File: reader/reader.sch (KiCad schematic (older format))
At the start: 63 parts, among them J1 USB_B_Mini, J2 swd, J3 Conn_01x06, J4 v_sup, Q1 CPH3350-TL-W, SW1 SW_Push, U1 BA33BC0FP-E2, U2 ST25R95, U3 STM32G051GxU, U4 FC2004C03-NSWBBW-91*E, Y1 27.12MHz

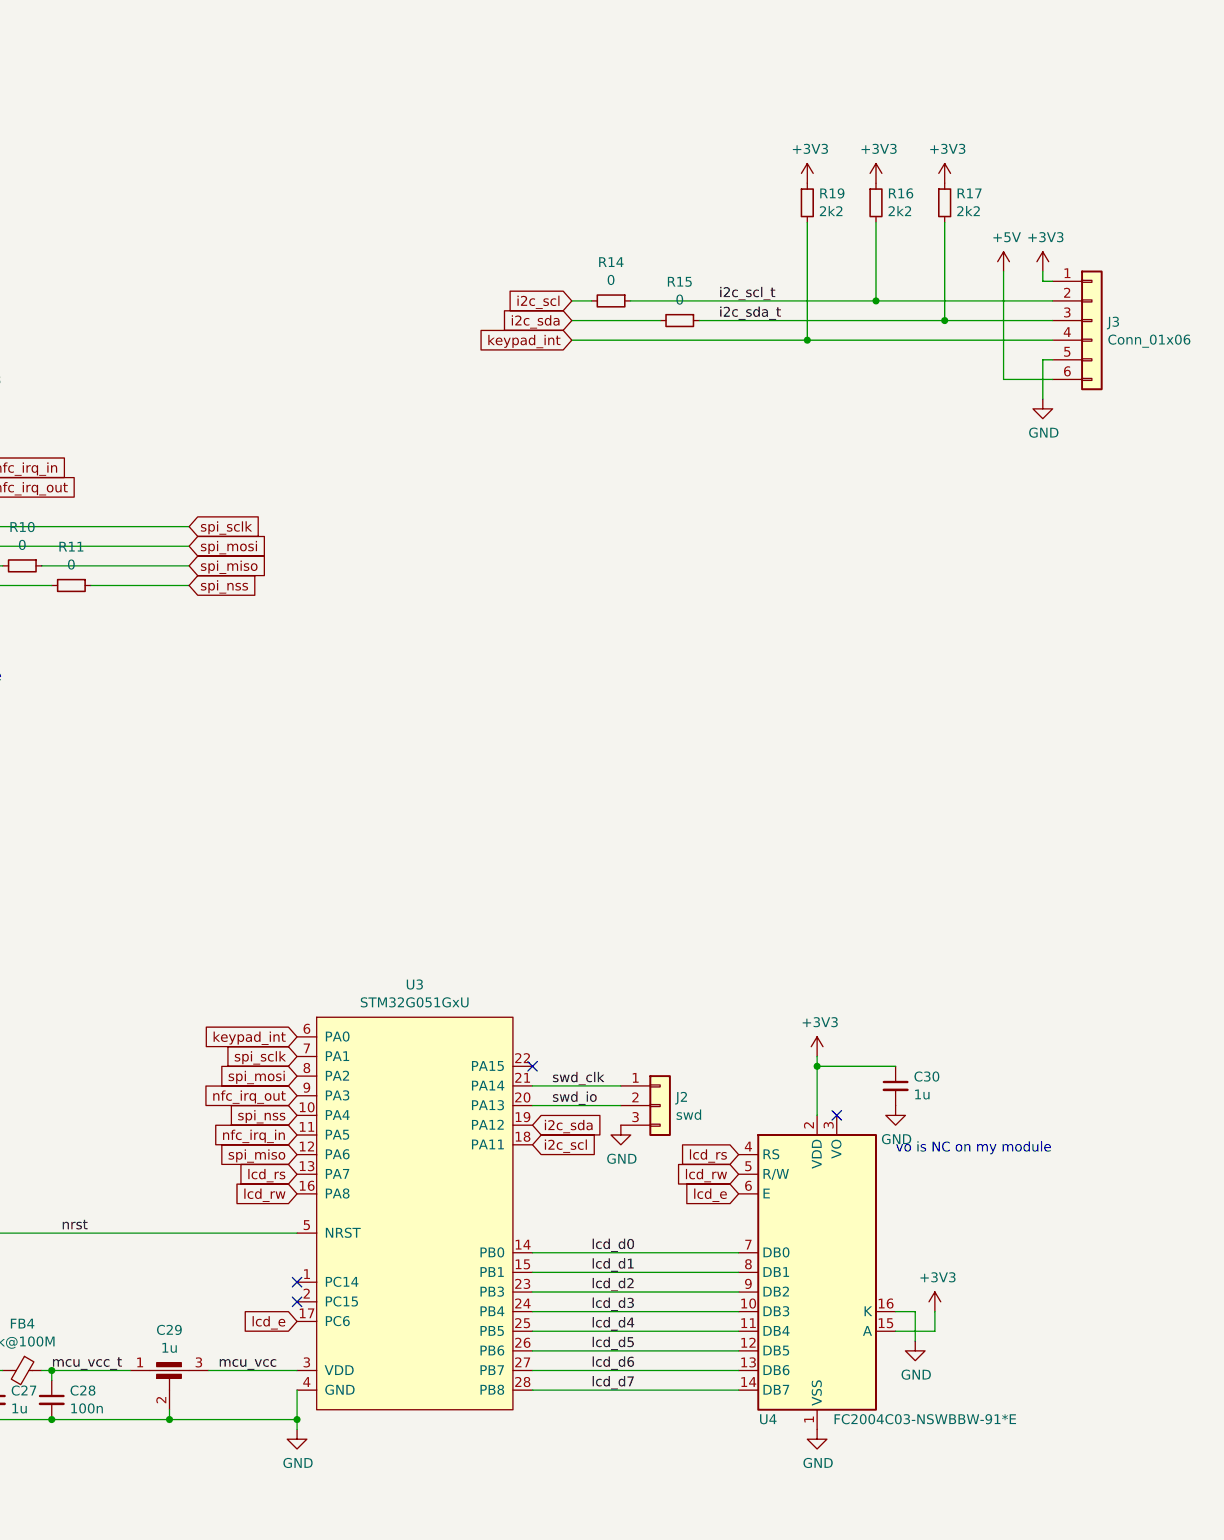
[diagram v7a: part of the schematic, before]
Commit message: Add proper mcu pinout and uart as output
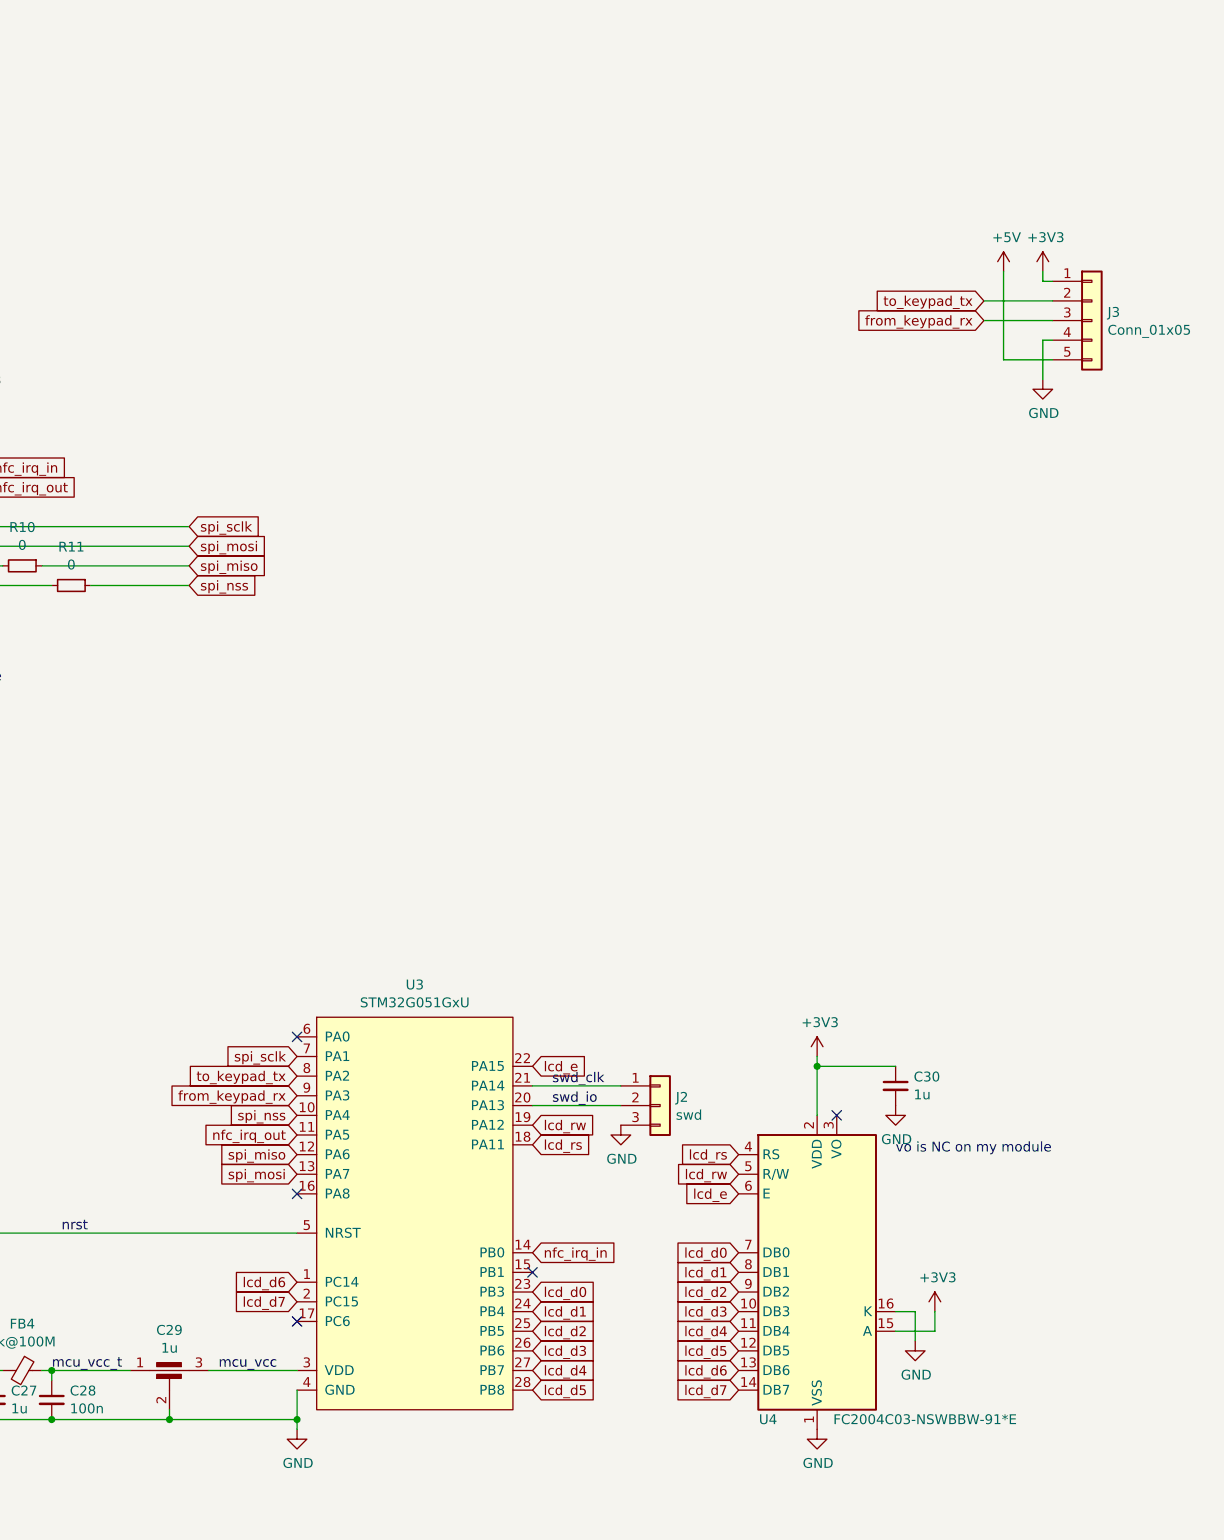
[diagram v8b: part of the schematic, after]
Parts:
- removed J3: Conn_01x06, Connector_PinHeader_2.54mm:PinHeader_1x06_P2.54mm_Vertical, symbol Connector_Generic:Conn_01x06
- removed R14, R15: 0, Resistor_SMD:R_0603_1608Metric_Pad1.05x0.95mm_HandSolder, symbol Device:R_Small
- removed R16, R17, R19: 2k2, Resistor_SMD:R_0603_1608Metric_Pad1.05x0.95mm_HandSolder, symbol Device:R_Small
- added J3: Conn_01x05, Connector_PinHeader_2.54mm:PinHeader_1x05_P2.54mm_Vertical, symbol Connector_Generic:Conn_01x05
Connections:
- net i2c_scl is gone; now on net lcd_rs: U3.18 (PA11)
- net i2c_sda is gone; now on net lcd_rw: U3.19 (PA12)
- net +3V3: now also J3.1 (Pin_1)
- net +5V: now also J3.5 (Pin_5)
- net GND: now also J3.4 (Pin_4)
- net lcd_d0: now also U3.23 (PB3); no longer U3.14 (PB0)
- net lcd_d1: now also U3.24 (PB4); no longer U3.15 (PB1)
- net lcd_d2: now also U3.25 (PB5); no longer U3.23 (PB3)
- net lcd_d3: now also U3.26 (PB6); no longer U3.24 (PB4)
- net lcd_d4: now also U3.27 (PB7); no longer U3.25 (PB5)
- net lcd_d5: now also U3.28 (PB8); no longer U3.26 (PB6)
- net lcd_d6: now also U3.1 (PC14); no longer U3.27 (PB7)
- net lcd_d7: now also U3.2 (PC15); no longer U3.28 (PB8)
- net lcd_e: now also U3.22 (PA15); no longer U3.17 (PC6)
- net lcd_rs: no longer U3.13 (PA7)
- net lcd_rw: no longer U3.16 (PA8)
- net nfc_irq_in: now also U3.14 (PB0); no longer U3.11 (PA5)
- net nfc_irq_out: now also U3.11 (PA5); no longer U3.9 (PA3)
- net spi_mosi: now also U3.13 (PA7); no longer U3.8 (PA2)
- net keypad_int: no longer names the net of U3.6 (PA0)
- new net from_keypad_rx: J3.3 (Pin_3), U3.9 (PA3)
- new net to_keypad_tx: J3.2 (Pin_2), U3.8 (PA2)
- no-connect marks 5 -> 6
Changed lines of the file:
@@
 	1    0    0    -1
 $EndComp
-Text GLabel 12050 2650 0    50   Input ~ 0
-i2c_sda
-Text GLabel 12050 2550 0    50   Input ~ 0
-i2c_scl
-$Comp
-L power:+3V3 #PWR031
-U 1 1 617ACEE2
-P 13600 1950
-F 0 "#PWR031" H 13600 1800 50  0001 C CNN
-F 1 "+3V3" H 13615 2123 50  0000 C CNN
-F 2 "" H 13600 1950 50  0001 C CNN
-F 3 "" H 13600 1950 50  0001 C CNN
-	1    13600 1950
-	1    0    0    -1
-$EndComp
-$Comp
-L Device:R_Small R16
-U 1 1 617AD187
-P 13600 2050
-F 0 "R16" H 13659 2096 50  0000 L CNN
-F 1 "2k2" H 13659 2005 50  0000 L CNN
-F 2 "Resistor_SMD:R_0603_1608Metric_Pad1.05x0.95mm_HandSolder" H 13600 2050 50  0001 C CNN
-F 3 "~" H 13600 2050 50  0001 C CNN
-	1    13600 2050
-	1    0    0    -1
-$EndComp
-$Comp
-L power:+3V3 #PWR032
-U 1 1 617B431C
-P 13950 1950
-F 0 "#PWR032" H 13950 1800 50  0001 C CNN
-F 1 "+3V3" H 13965 2123 50  0000 C CNN
-F 2 "" H 13950 1950 50  0001 C CNN
-F 3 "" H 13950 1950 50  0001 C CNN
-	1    13950 1950
-	1    0    0    -1
-$EndComp
-$Comp
-L Device:R_Small R17
-U 1 1 617B4322
-P 13950 2050
-F 0 "R17" H 14009 2096 50  0000 L CNN
-F 1 "2k2" H 14009 2005 50  0000 L CNN
-F 2 "Resistor_SMD:R_0603_1608Metric_Pad1.05x0.95mm_HandSolder" H 13950 2050 50  0001 C CNN
-F 3 "~" H 13950 2050 50  0001 C CNN
-	1    13950 2050
-	1    0    0    -1
-$EndComp
-Wire Wire Line
-	13600 2150 13600 2550
 $Comp
 L power:GND #PWR034
 U 1 1 617F51EA
-P 14450 3050
-F 0 "#PWR034" H 14450 2800 50  0001 C CNN
-F 1 "GND" H 14455 2877 50  0000 C CNN
-F 2 "" H 14450 3050 50  0001 C CNN
-F 3 "" H 14450 3050 50  0001 C CNN
-	1    14450 3050
-	1    0    0    -1
-$EndComp
-Text GLabel 12050 2750 0    50   Input ~ 0
-keypad_int
-Wire Wire Line
-	13950 2150 13950 2650
+P 14450 2950
+F 0 "#PWR034" H 14450 2700 50  0001 C CNN
+F 1 "GND" H 14455 2777 50  0000 C CNN
+F 2 "" H 14450 2950 50  0001 C CNN
+F 3 "" H 14450 2950 50  0001 C CNN
+	1    14450 2950
+	1    0    0    -1
+$EndComp
 $Comp
 L Connector_Generic:Conn_01x02 J4
@@
 Wire Wire Line
 	7300 4900 7400 4900
-Text GLabel 10650 6300 0    50   Input ~ 0
-keypad_int
-NoConn ~ 11850 6450
 Wire Wire Line
 	10200 8000 10650 8000
@@
 Text Label 10250 8000 0    50   ~ 0
 mcu_vcc
-Text GLabel 11850 6850 2    50   Input ~ 0
-i2c_scl
-Text GLabel 11850 6750 2    50   Input ~ 0
-i2c_sda
 Text Label 11950 6650 0    50   ~ 0
 swd_io
@@
 Wire Wire Line
 	10650 8100 10650 8250
-Text GLabel 10650 7750 0    50   Input ~ 0
-lcd_e
-Text GLabel 10650 7100 0    50   Input ~ 0
+Text GLabel 11850 6750 2    50   Input ~ 0
 lcd_rw
-Text GLabel 10650 7000 0    50   Input ~ 0
+Text GLabel 11850 6850 2    50   Input ~ 0
 lcd_rs
-Text Label 12150 8100 0    50   ~ 0
-lcd_d7
-Text Label 12150 8000 0    50   ~ 0
-lcd_d6
-Text Label 12150 7900 0    50   ~ 0
-lcd_d5
-Text Label 12150 7800 0    50   ~ 0
-lcd_d4
-Text Label 12150 7700 0    50   ~ 0
-lcd_d3
-Text Label 12150 7600 0    50   ~ 0
-lcd_d2
-Text Label 12150 7500 0    50   ~ 0
-lcd_d1
-Text Label 12150 7400 0    50   ~ 0
-lcd_d0
+Text GLabel 11850 7400 2    50   Input ~ 0
+nfc_irq_in
 Text GLabel 10650 6800 0    50   Input ~ 0
-nfc_irq_in
-Text GLabel 10650 6600 0    50   Input ~ 0
 nfc_irq_out
 Text GLabel 10650 6900 0    50   Input ~ 0
@@
 Text GLabel 10650 6700 0    50   Input ~ 0
 spi_nss
-Text GLabel 10650 6500 0    50   Input ~ 0
+Text GLabel 10650 7000 0    50   Input ~ 0
 spi_mosi
 Text GLabel 10650 6400 0    50   Input ~ 0
 spi_sclk
-Wire Wire Line
-	11850 8100 12900 8100
-Wire Wire Line
-	12900 8000 11850 8000
-Wire Wire Line
-	11850 7900 12900 7900
-Wire Wire Line
-	11850 7800 12900 7800
-Wire Wire Line
-	12900 7700 11850 7700
-Wire Wire Line
-	11850 7600 12900 7600
-Wire Wire Line
-	12900 7500 11850 7500
-Wire Wire Line
-	11850 7400 12900 7400
 Wire Wire Line
 	8100 7300 8100 7350
@@
 	1    0    0    -1
 $EndComp
-$Comp
-L Connector_Generic:Conn_01x06 J3
-U 1 1 61680C40
-P 14700 2650
-F 0 "J3" H 14780 2642 50  0000 L CNN
-F 1 "Conn_01x06" H 14780 2551 50  0000 L CNN
-F 2 "Connector_PinHeader_2.54mm:PinHeader_1x06_P2.54mm_Vertical" H 14700 2650 50  0001 C CNN
-F 3 "~" H 14700 2650 50  0001 C CNN
-	1    14700 2650
-	1    0    0    -1
-$EndComp
 Wire Wire Line
 	14450 2450 14450 2400
@@
 	14450 2450 14500 2450
 Wire Wire Line
-	13600 2550 14500 2550
-Wire Wire Line
-	13950 2650 14500 2650
-Wire Wire Line
 	7650 2900 8100 2900
 Wire Wire Line
@@
 Wire Wire Line
 	4200 1350 4600 1350
-Wire Wire Line
-	14450 3050 14450 2850
-Wire Wire Line
-	14450 2850 14500 2850
-Wire Wire Line
-	14500 2950 14250 2950
-Wire Wire Line
-	14250 2400 14250 2950
-NoConn ~ 10650 7550
-NoConn ~ 10650 7650
 Wire Wire Line
 	8600 7300 10650 7300
@@
 Wire Wire Line
 	10000 8250 10650 8250
-Text Label 12800 2650 0    50   ~ 0
-i2c_sda_t
-Text Label 12800 2550 0    50   ~ 0
-i2c_scl_t
-Wire Wire Line
-	12500 2650 12050 2650
-Wire Wire Line
-	12150 2550 12050 2550
-$Comp
-L Device:R_Small R15
-U 1 1 617FEC6C
-P 12600 2650
-F 0 "R15" V 12404 2650 50  0000 C CNN
-F 1 "0" V 12495 2650 50  0000 C CNN
-F 2 "Resistor_SMD:R_0603_1608Metric_Pad1.05x0.95mm_HandSolder" H 12600 2650 50  0001 C CNN
-F 3 "~" H 12600 2650 50  0001 C CNN
-	1    12600 2650
-	0    1    1    0
-$EndComp
-$Comp
-L Device:R_Small R14
-U 1 1 617FEA2B
-P 12250 2550
-F 0 "R14" V 12054 2550 50  0000 C CNN
-F 1 "0" V 12145 2550 50  0000 C CNN
-F 2 "Resistor_SMD:R_0603_1608Metric_Pad1.05x0.95mm_HandSolder" H 12250 2550 50  0001 C CNN
-F 3 "~" H 12250 2550 50  0001 C CNN
-	1    12250 2550
-	0    1    1    0
-$EndComp
-Wire Wire Line
-	12050 2750 13250 2750
-Wire Wire Line
-	12700 2650 13950 2650
-Connection ~ 13950 2650
-Connection ~ 13600 2550
-$Comp
-L power:+3V3 #PWR0103
-U 1 1 616B91B8
-P 13250 1950
-F 0 "#PWR0103" H 13250 1800 50  0001 C CNN
-F 1 "+3V3" H 13265 2123 50  0000 C CNN
-F 2 "" H 13250 1950 50  0001 C CNN
-F 3 "" H 13250 1950 50  0001 C CNN
-	1    13250 1950
-	1    0    0    -1
-$EndComp
-$Comp
-L Device:R_Small R19
-U 1 1 616B91BE
-P 13250 2050
-F 0 "R19" H 13309 2096 50  0000 L CNN
-F 1 "2k2" H 13309 2005 50  0000 L CNN
-F 2 "Resistor_SMD:R_0603_1608Metric_Pad1.05x0.95mm_HandSolder" H 13250 2050 50  0001 C CNN
-F 3 "~" H 13250 2050 50  0001 C CNN
-	1    13250 2050
-	1    0    0    -1
-$EndComp
-Wire Wire Line
-	12350 2550 13600 2550
-Wire Wire Line
-	13250 2150 13250 2750
-Connection ~ 13250 2750
-Wire Wire Line
-	13250 2750 14500 2750
+Text GLabel 11850 7700 2    50   Input ~ 0
+lcd_d1
+Text GLabel 11850 6450 2    50   Input ~ 0
+lcd_e
+Text GLabel 11850 7600 2    50   Input ~ 0
+lcd_d0
+NoConn ~ 10650 7750
+Text GLabel 12900 7500 0    50   Input ~ 0
+lcd_d1
+Text GLabel 12900 7600 0    50   Input ~ 0
+lcd_d2
+Text GLabel 12900 7700 0    50   Input ~ 0
+lcd_d3
+Text GLabel 12900 7800 0    50   Input ~ 0
+lcd_d4
+Text GLabel 12900 7900 0    50   Input ~ 0
+lcd_d5
+Text GLabel 12900 8000 0    50   Input ~ 0
+lcd_d6
+Text GLabel 12900 8100 0    50   Input ~ 0
+lcd_d7
+Text GLabel 12900 7400 0    50   Input ~ 0
+lcd_d0
+NoConn ~ 11850 7500
+NoConn ~ 10650 6300
+Text GLabel 10650 6500 0    50   Input ~ 0
+to_keypad_tx
+Text GLabel 10650 6600 0    50   Input ~ 0
+from_keypad_rx
+NoConn ~ 10650 7100
+Text GLabel 14150 2550 0    50   Input ~ 0
+to_keypad_tx
+Text GLabel 14150 2650 0    50   Input ~ 0
+from_keypad_rx
+$Comp
+L Connector_Generic:Conn_01x05 J3
+U 1 1 616F7D49
+P 14700 2650
+F 0 "J3" H 14780 2692 50  0000 L CNN
+F 1 "Conn_01x05" H 14780 2601 50  0000 L CNN
+F 2 "Connector_PinHeader_2.54mm:PinHeader_1x05_P2.54mm_Vertical" H 14700 2650 50  0001 C CNN
+F 3 "~" H 14700 2650 50  0001 C CNN
+	1    14700 2650
+	1    0    0    -1
+$EndComp
+Wire Wire Line
+	14250 2400 14250 2850
+Wire Wire Line
+	14450 2750 14500 2750
+Wire Wire Line
+	14450 2750 14450 2950
+Wire Wire Line
+	14250 2850 14500 2850
+Wire Wire Line
+	14150 2550 14500 2550
+Wire Wire Line
+	14500 2650 14150 2650
+Text GLabel 11850 7800 2    50   Input ~ 0
+lcd_d2
+Text GLabel 11850 7900 2    50   Input ~ 0
+lcd_d3
+Text GLabel 11850 8000 2    50   Input ~ 0
+lcd_d4
+Text GLabel 11850 8100 2    50   Input ~ 0
+lcd_d5
+Text GLabel 10650 7550 0    50   Input ~ 0
+lcd_d6
+Text GLabel 10650 7650 0    50   Input ~ 0
+lcd_d7
 $EndSCHEMATC
